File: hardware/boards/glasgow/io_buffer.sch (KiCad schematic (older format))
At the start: 59 parts, among them J2 Conn_02x10_Odd_Even, J6 Conn_01x08, J7 Conn_01x08, U10 DAC081C081CIMK, U11 TPS73101DBV, U16 SN74LVC1T45DRL, U17 SN74LVC1T45DRL, U18 SN74LVC1T45DRL, U19 PCA6408APW, U19 SN74LVC1T45DRL, U20 SN74LVC1T45DRL, U21 SN74LVC1T45DRL, U33 MG2040, U5 SN74LVC1T45DRL, U6 SN74LVC1T45DRL, U9 ADC081C021CIMM

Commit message: revC2: replace ADC with INA233 voltage & current monitor
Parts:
- removed C37: 12n, Capacitor_SMD:C_0402_1005Metric, symbol Device:C
- removed R20, R21: 10k, Resistor_SMD:R_0402_1005Metric, symbol Device:R
- removed U9: ADC081C021CIMM, Package_SO:MSOP-8_3x3mm_P0.65mm, symbol Analog_ADC:ADC081C021CIMM
- added C58: u1, Capacitor_SMD:C_0402_1005Metric, symbol Device:C
- added D17: CDSOD323-T36S, Diode_SMD:D_SOD-323, symbol Device:D_Zener
- added D19: BAT54CW, Package_TO_SOT_SMD:SOT-323_SC-70, symbol Diode:BAT54CW
- added R26: 20k, Resistor_SMD:R_0402_1005Metric, symbol Device:R
- added R30, R54: 4r7, Resistor_SMD:R_0402_1005Metric, symbol Device:R
- added U21: INA233, Package_SO:VSSOP-10_3x3mm_P0.5mm, symbol Analog_ADC:INA233
- R49: value 0.68 -> 0.47; 1b2-bom-key res-0603-0_68 -> res-0603-0_47; MPN CRL0603-JW-R680ELF -> CRL0603-JW-R470ELF
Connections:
- net labels added: VIO_EN
- net labels removed: VSAMP
- wire segments 300 -> 317
- no-connect marks 11 -> 12
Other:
- note added: "-3dB @\n169 kHz"
- note added: "Abs. max\n-0.3 < Vbus < 40\n"
- note added: "Addr (ADRADC=L): 1000000\nAddr (ADRADC=H): 1000001\nAddr (ADRADC=SDA): 1000010\nAddr (ADRADC=SCL): 1000011"
- note added: "Imax @ 3V3 = 0.4 mA"
- note added: "Shunt diff input range\n-81.9 to 81.9 mV\n= 174 mA max"
- note removed: "Addr (ADR=X): 1010100\nAddr (ADR=L): 1010101\nAddr (ADR=H): 1010110"
- note removed: "Csamp = 20 pF\nBits = 8\nCext = (2**(Bits+1)-1)*Csamp = 10.2 nF (min)\nGamma = ln(2**(Bits+1)) = 6.24\nFreq = 1 ksps\nRsource = 1/(Gamma*Cext*Freq) = 15.7 kohm (max)\nRdiv = 2*Rsource = 31.4 kohm (max)"
- note removed: "Functional equivalents:\n- ADC101C021CIMM\n- ADC121C021CIMM"
- note removed: "Imax @ 3V3 = 0.73 mA"
- moved on the sheet: C31, C45, D14, R27, R46, TP18, U13

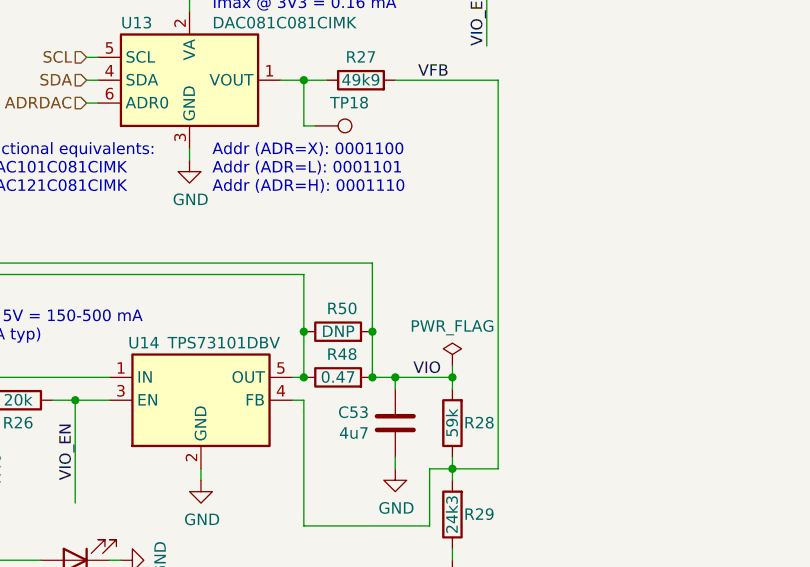
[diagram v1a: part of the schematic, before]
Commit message: revC2: documentation improvements & small beautifications
schematics part of #165 done
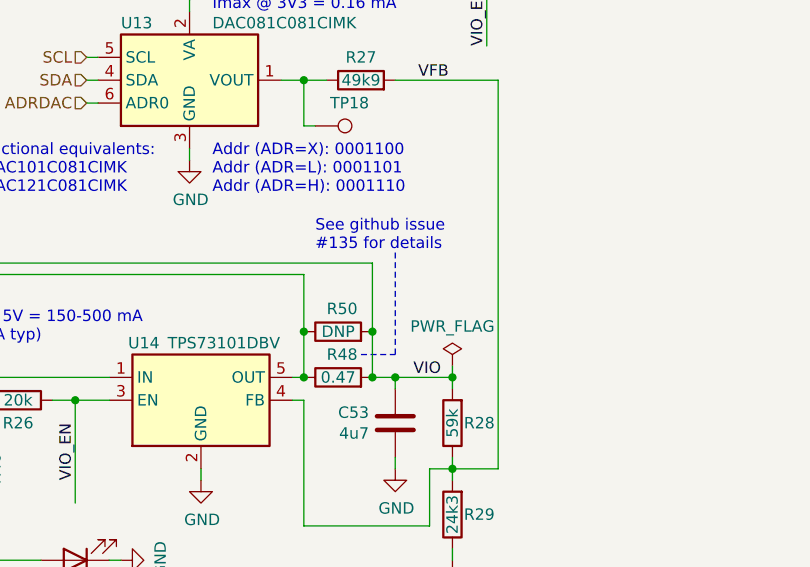
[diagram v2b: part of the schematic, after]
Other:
- note added: "See github issue \n#135 for details"

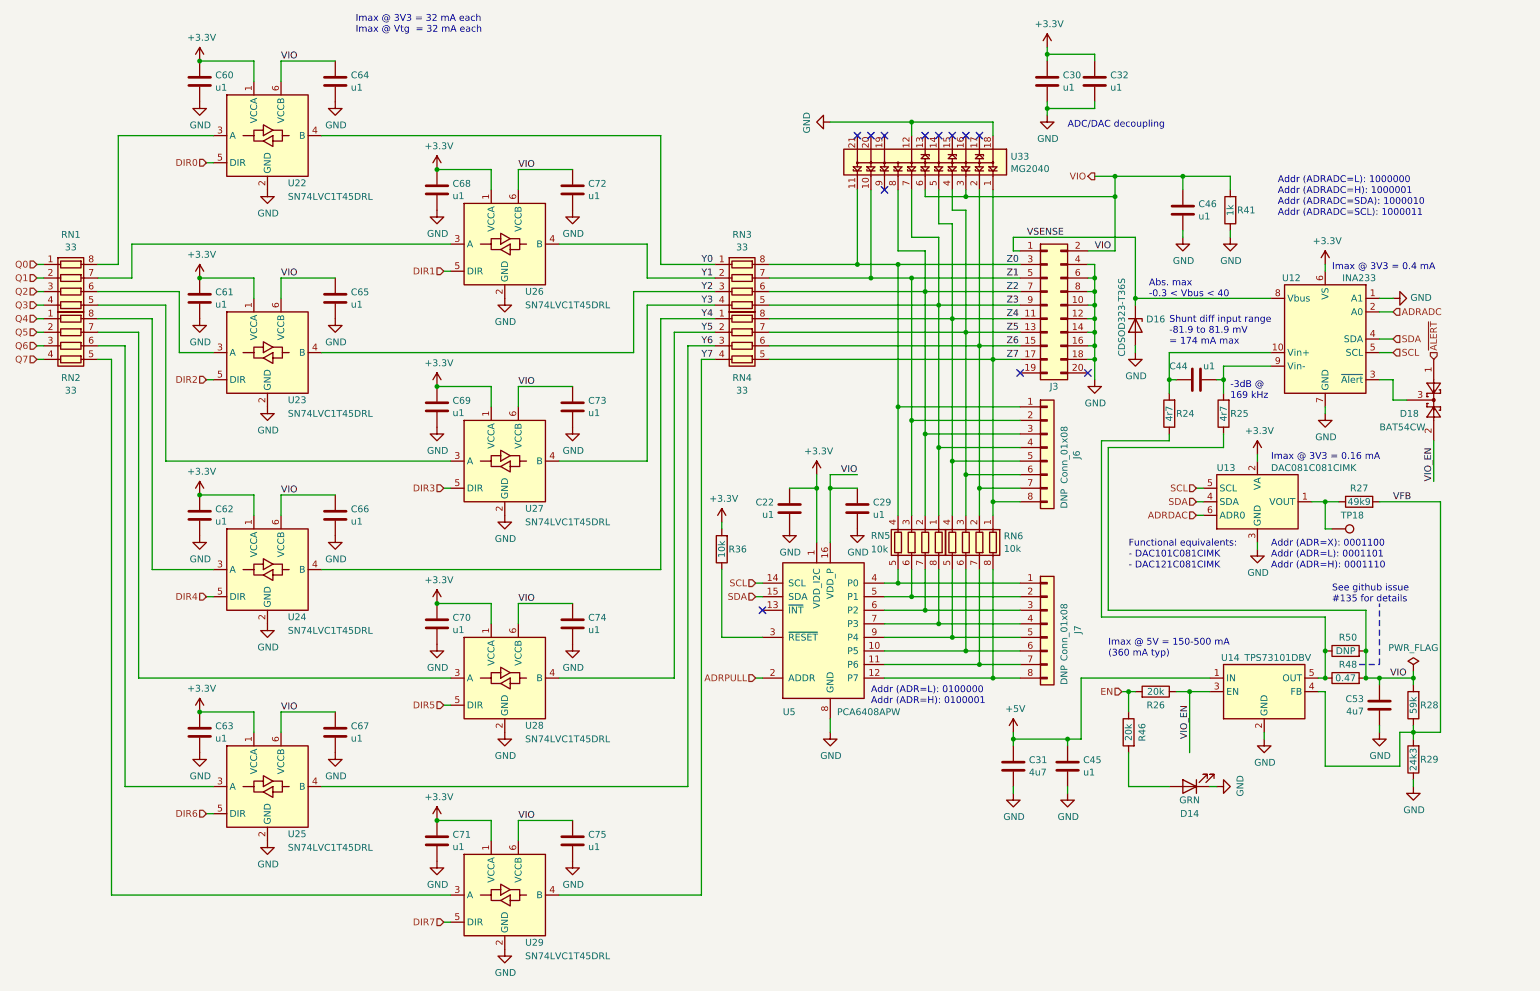
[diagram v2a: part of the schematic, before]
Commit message: revC2: remove left-over traces, place new footprints
Also add new footprints where necessary, fix a silkscreen bug
Layout for new components still TODO
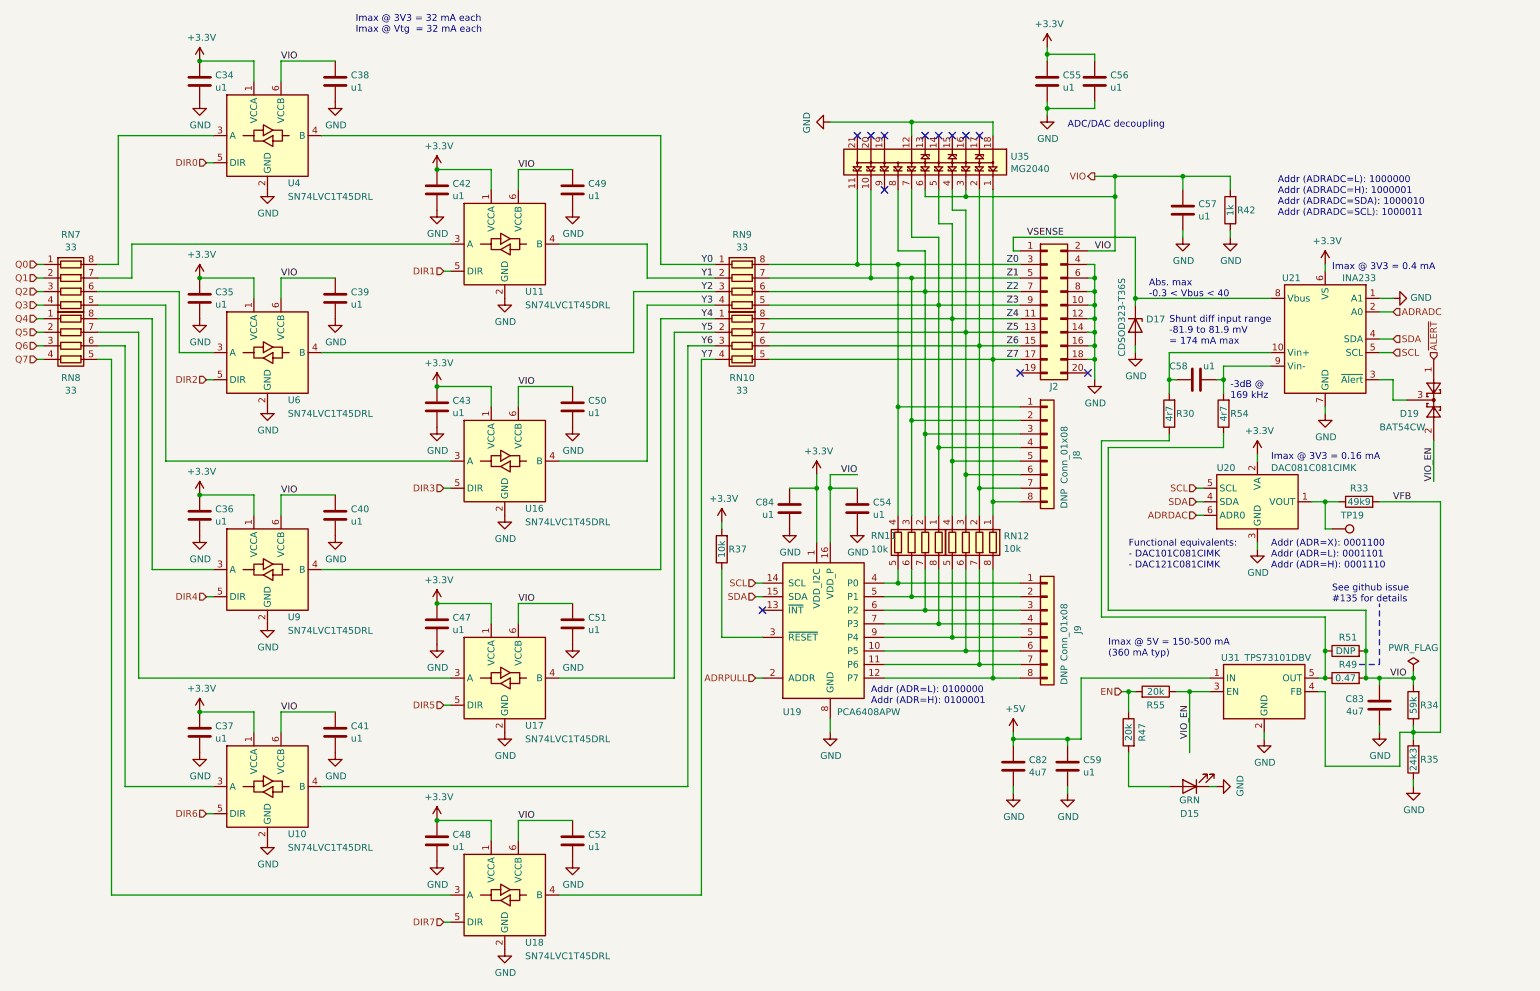
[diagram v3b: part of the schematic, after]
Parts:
- D17: footprint Diode_SMD:D_SOD-323 -> Glasgow:D_SOD-323
- D19: footprint Package_TO_SOT_SMD:SOT-323_SC-70 -> Glasgow:SOT-323_SC-70

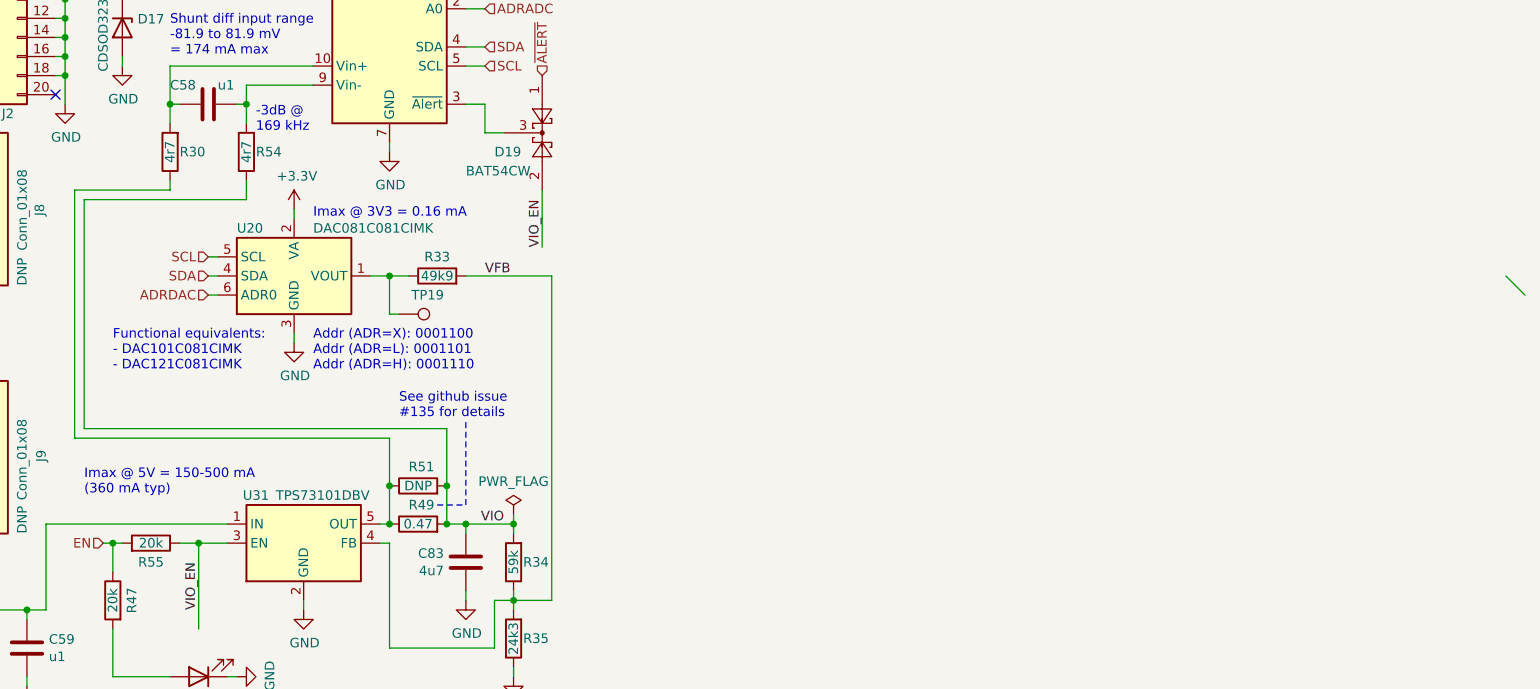
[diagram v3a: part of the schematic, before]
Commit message: revC2: schematics fixup
Add manufacturer names & MPNs, remove stray wire, uppercase R in resistor values
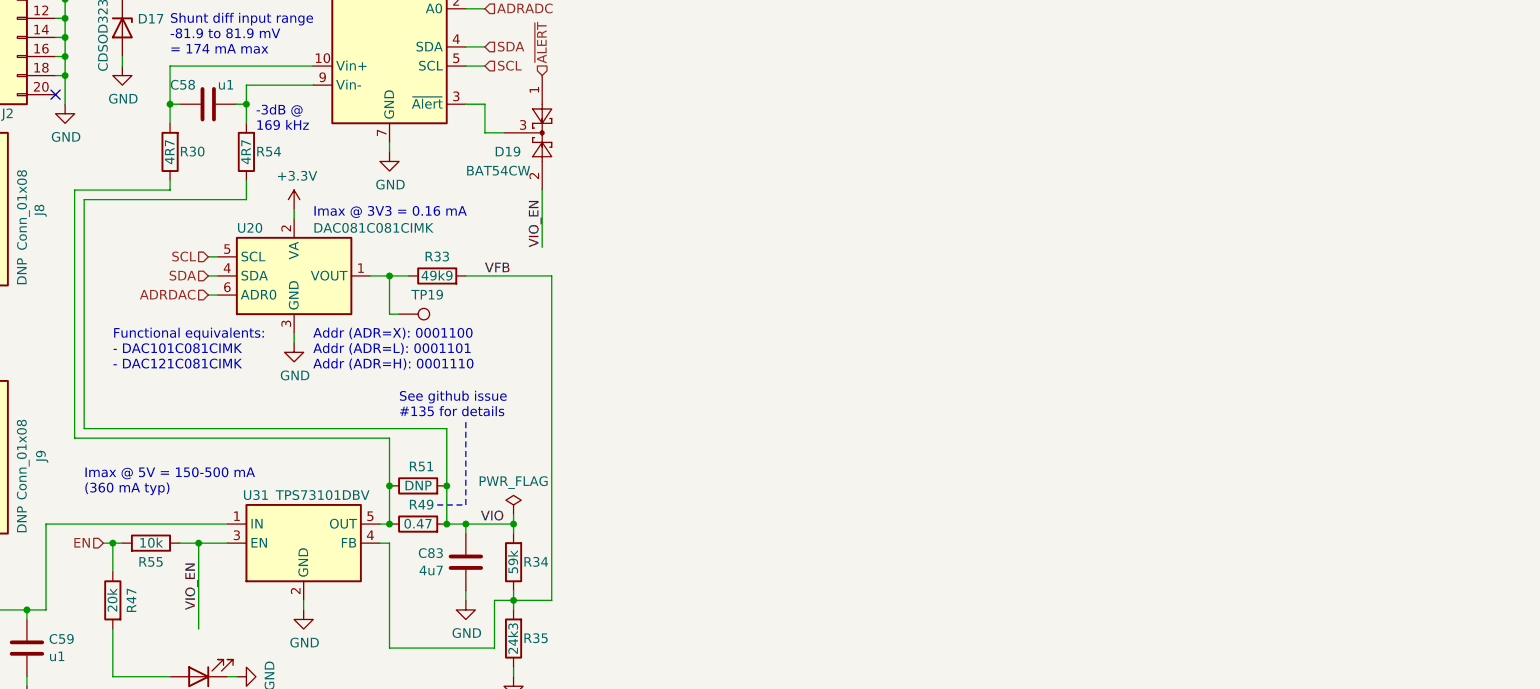
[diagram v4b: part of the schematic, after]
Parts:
- D17: MPN (none) -> CDSOD323-T36S; Mfg (none) -> Bourns
- D19: MPN (none) -> BAT54CW-7-F; Mfg (none) -> Diodes Inc.
- R26: value 20k -> 10k; 1b2-bom-key res-0402-20k -> res-0402-10k; MPN RC0402FR-1320KL -> RC0402FR-1310KL
- R30, R54: value 4r7 -> 4R7; 1b2-bom-key res-0402-4r7 -> res-0402-4R7
- U21: MPN (none) -> INA233AIDGSR; Mfg (none) -> Texas Instruments
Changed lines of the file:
@@
 Wire Wire Line
 	1350 7050 3850 7050
-Entry Wire Line
-	16150 4150 16250 4250
 $Comp
 L Glasgow:PCA6408APW U?
@@
 F 2 "Package_SO:VSSOP-10_3x3mm_P0.5mm" H 11100 2500 50  0001 C CNN
 F 3 "https://www.ti.com/lit/ds/symlink/ina233.pdf" H 10650 2850 50  0001 C CNN
+F 4 "Texas Instruments" H 10300 2950 50  0001 C CNN "Mfg"
+F 5 "INA233AIDGSR" H 10300 2950 50  0001 C CNN "MPN"
 	1    10300 2950
 	1    0    0    -1
@@
 F 2 "Glasgow:D_SOD-323" H 8900 2850 50  0001 C CNN
 F 3 "https://bourns.com/docs/product-datasheets/cdsod323-txxsc.pdf" H 8900 2850 50  0001 C CNN
+F 4 "Bourns" V 8900 2850 50  0001 C CNN "Mfg"
+F 5 "CDSOD323-T36S" V 8900 2850 50  0001 C CNN "MPN"
 	1    8900 2850
 	0    1    1    0
@@
 AR Path="/5C7B59B0/5C9E338E/5F1A23B9" Ref="R25"  Part="1"
 F 0 "R54" H 9500 3500 50  0000 R CNN
-F 1 "4r7" V 9550 3500 50  0000 C CNN
+F 1 "4R7" V 9550 3500 50  0000 C CNN
 F 2 "Resistor_SMD:R_0402_1005Metric" V 9480 3500 50  0001 C CNN
 F 3 "https://www.mouser.com/datasheet/2/447/PYu-RC_Group_51_RoHS_L_10-1527934.pdf" H 9550 3500 50  0001 C CNN
 F 4 "Yageo" H 3400 -1450 50  0001 C CNN "Mfg"
 F 5 "RC0402FR-074R7L" H 3400 -1450 50  0001 C CNN "MPN"
-F 6 "res-0402-4r7" H 9550 3500 50  0001 C CNN "1b2-bom-key"
+F 6 "res-0402-4R7" H 9550 3500 50  0001 C CNN "1b2-bom-key"
 	1    9550 3500
 	-1   0    0    1
@@
 AR Path="/5C7B59B0/5C9E338E/5F1A3005" Ref="R24"  Part="1"
 F 0 "R30" H 9100 3500 50  0000 R CNN
-F 1 "4r7" V 9150 3500 50  0000 C CNN
+F 1 "4R7" V 9150 3500 50  0000 C CNN
 F 2 "Resistor_SMD:R_0402_1005Metric" V 9080 3500 50  0001 C CNN
 F 3 "https://www.mouser.com/datasheet/2/447/PYu-RC_Group_51_RoHS_L_10-1527934.pdf" H 9150 3500 50  0001 C CNN
 F 4 "Yageo" H 3000 -1450 50  0001 C CNN "Mfg"
 F 5 "RC0402FR-074R7L" H 3000 -1450 50  0001 C CNN "MPN"
-F 6 "res-0402-4r7" H 9150 3500 50  0001 C CNN "1b2-bom-key"
+F 6 "res-0402-4R7" H 9150 3500 50  0001 C CNN "1b2-bom-key"
 	1    9150 3500
 	-1   0    0    1
@@
 AR Path="/5C7B59B0/5C9E337E/5F2A58A0" Ref="R55"  Part="1"
 F 0 "R55" V 8950 5550 50  0000 C CNN
-F 1 "20k" V 9050 5550 50  0000 C CNN
+F 1 "10k" V 9050 5550 50  0000 C CNN
 F 2 "Resistor_SMD:R_0402_1005Metric" V 8980 5550 50  0001 C CNN
 F 3 "https://www.mouser.com/datasheet/2/447/PYu-RC_Group_51_RoHS_L_10-1527934.pdf" H 9050 5550 50  0001 C CNN
 F 4 "Yageo" H -850 4450 50  0001 C CNN "Mfg"
-F 5 "RC0402FR-1320KL" H -850 4450 50  0001 C CNN "MPN"
-F 6 "res-0402-20k" H 9050 5550 50  0001 C CNN "1b2-bom-key"
+F 5 "RC0402FR-1310KL" H -850 4450 50  0001 C CNN "MPN"
+F 6 "res-0402-10k" H 9050 5550 50  0001 C CNN "1b2-bom-key"
 	1    9050 5550
 	0    1    -1   0
@@
 F 1 "BAT54CW" V 11300 3000 50  0000 L CNN
 F 2 "Glasgow:SOT-323_SC-70" H 11175 3525 50  0001 L CNN
-F 3 "https://assets.nexperia.com/documents/data-sheet/BAT54W_SER.pdf" H 11020 3400 50  0001 C CNN
+F 3 "https://www.diodes.com/assets/Datasheets/ds30065.pdf" H 11020 3400 50  0001 C CNN
+F 4 "Diodes Inc." V 11100 3400 50  0001 C CNN "Mfg"
+F 5 "BAT54CW-7-F" V 11100 3400 50  0001 C CNN "MPN"
 	1    11100 3400
 	0    1    1    0
